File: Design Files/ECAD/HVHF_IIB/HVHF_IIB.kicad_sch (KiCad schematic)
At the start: 17 parts, among them Q1 PNP, Q2 NPN, Q3 NPN, Q4 NPN, Q5 NPN, Q6 PNP

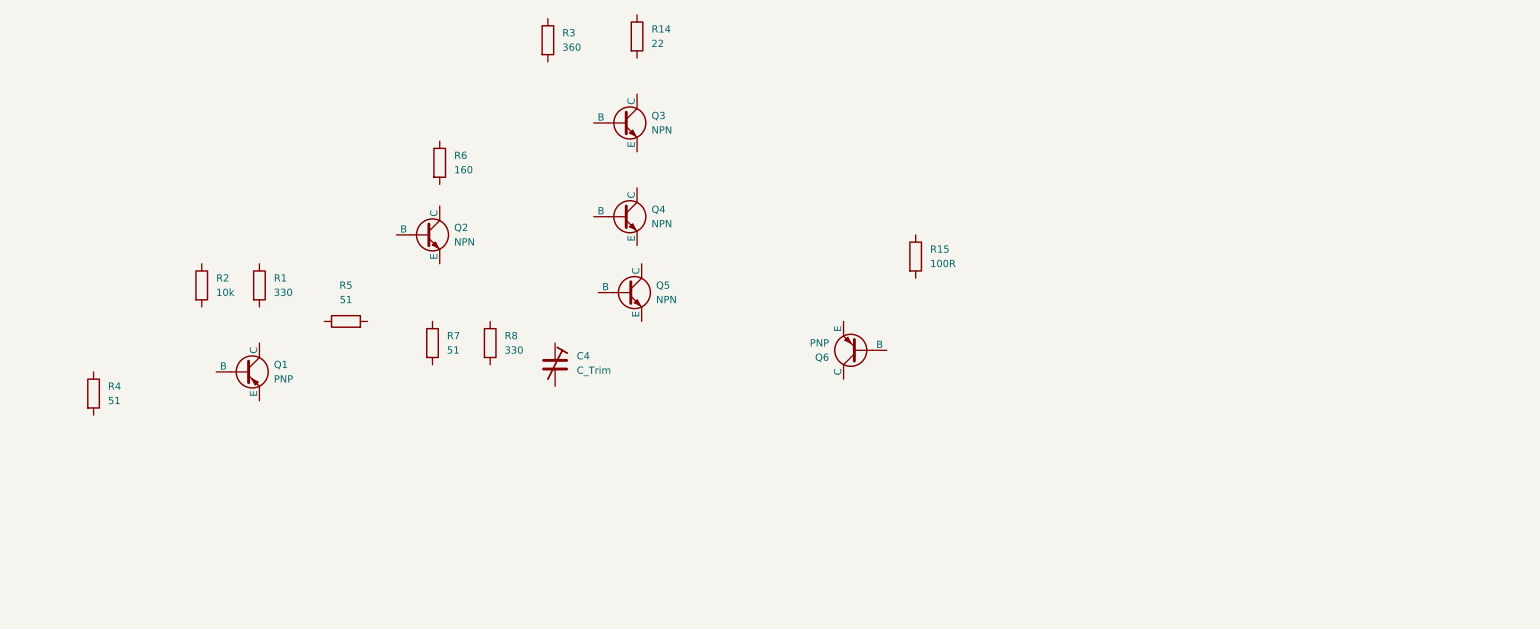
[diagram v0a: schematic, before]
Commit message: schematic work
adds components
some foot prints
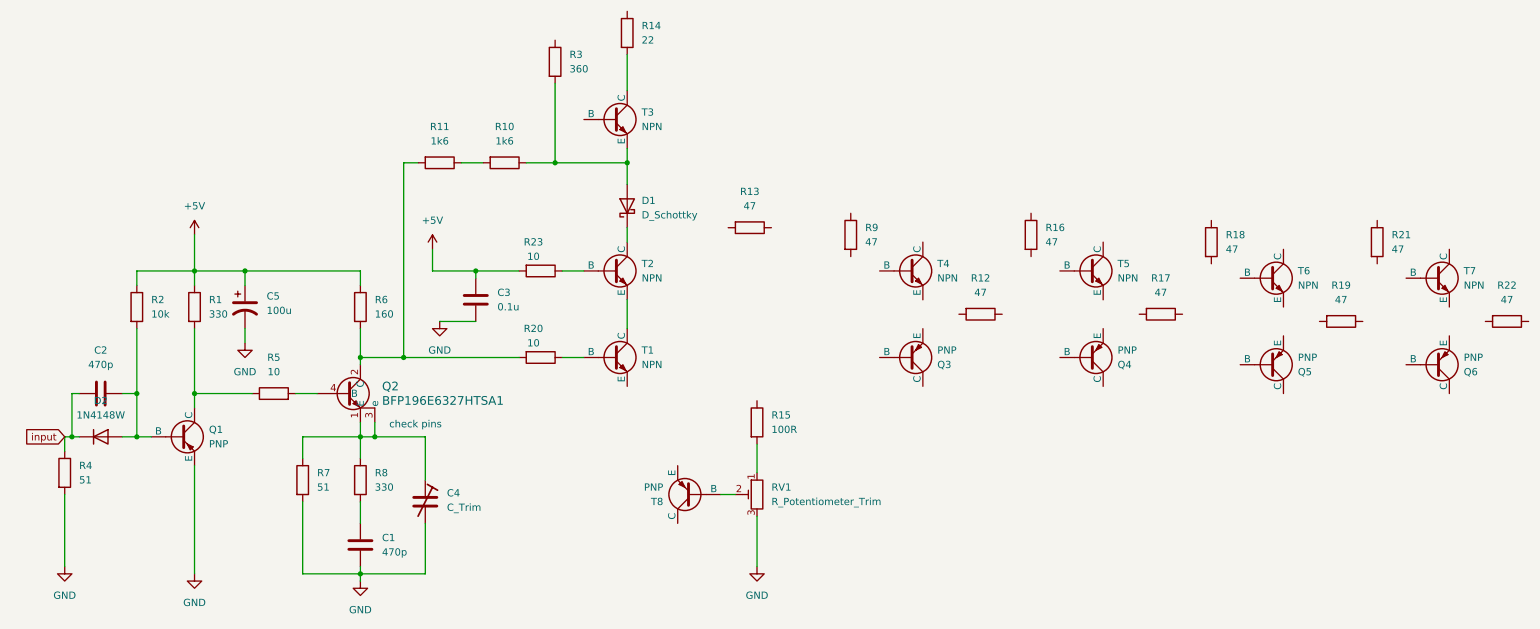
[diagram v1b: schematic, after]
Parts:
- removed Q2: NPN, symbol Simulation_SPICE:NPN
- added C1, C2: 470p, Capacitor_SMD:C_0805_2012Metric_Pad1.18x1.45mm_HandSolder, symbol Device:C
- added C3: 0.1u, Capacitor_SMD:C_0805_2012Metric_Pad1.18x1.45mm_HandSolder, symbol Device:C
- added C5: 100u, symbol Device:C_Polarized_US
- added D1: D_Schottky, symbol Device:D_Schottky
- added D2: 1N4148W, Diode_SMD:D_SOD-123, symbol Diode:1N4148W
- added Q2: BFP196E6327HTSA1, Library:TRANS_BFP196E6327HTSA1_INF, symbol New_Library:BFP196E6327HTSA1
- added Q3, Q4, Q5, Q6: PNP, symbol Simulation_SPICE:PNP
- added R10, R11: 1k6, Resistor_SMD:R_2512_6332Metric, symbol Device:R
- added R12, R13, R16, R17, R18, R19, R21, R22, R9: 47, Resistor_SMD:R_0805_2012Metric_Pad1.20x1.40mm_HandSolder, symbol Device:R
- added R20, R23: 10, Resistor_SMD:R_0805_2012Metric_Pad1.20x1.40mm_HandSolder, symbol Device:R
- added RV1: R_Potentiometer_Trim, Library:POT_3296W, symbol Device:R_Potentiometer_Trim
- added T4, T5, T6, T7: NPN, symbol Simulation_SPICE:NPN
- Q1: footprint (none) -> Package_TO_SOT_SMD:SOT-23-3
- R5: value 51 -> 10
- T1: renamed from Q5; footprint (none) -> Package_TO_SOT_SMD:SOT-223
- renumbered Q4 to T2, Q3 to T3, Q6 to T8
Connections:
- net at T2.1 (C): now also D1.1 (K)
- net at T2.2 (B): now also R23.1
- net at T2.3 (E): now also T1.1 (C)
- net +5V: now reaches R2.1
- net +5V: now also R1.1, R6.1, C3.1, C5.1, R23.2
- net at R2.2: now also Q1.2 (B), C2.2, D2.2 (A)
- net at R5.1: now also Q1.1 (C), R1.2
- net at R5.2: now also Q2.4 (B)
- net at R15.2: now also RV1.1
- net at C4.1: now also R7.1, R8.1, Q2.1 (E), Q2.3 (e)
- net GND: now reaches C4.2
- net GND: now also Q1.3 (E), R4.2, R7.2, C1.2, C3.2, C5.2, RV1.3
- net at R3.2: now also T3.3 (E), D1.2 (A), R10.1
- net input: now reaches R4.1
- net input: now also C2.1, D2.1 (K)
- net at R6.2: now also Q2.2 (C), R11.2, R20.2
- net at T3.1 (C): now also R14.2
- net at T1.2 (B): now also R20.1
- net at T8.2 (B): now also RV1.2
- net at R8.2: now also C1.1
- new net: R10.2, R11.1
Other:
- note added: "check pins"
- moved on the sheet: C4, Q1, R1, R14, R15, R2, R3, R4, R5, R6, R7, R8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
